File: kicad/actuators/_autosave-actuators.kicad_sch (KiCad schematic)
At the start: 41 parts, among them J10 Conn_01x03, J11 Conn_01x03, J12 Conn_01x03, J13 Conn_01x03, J18 6V_IN, J19 3V3_IN, J5 Conn_02x03_Odd_Even, J6 Conn_01x06, J7 Conn_01x03, J8 Conn_01x03, J9 Conn_01x03, U5 SN65HVD230, U6 STM32G431R6Tx, U7 DRV8874PWPR

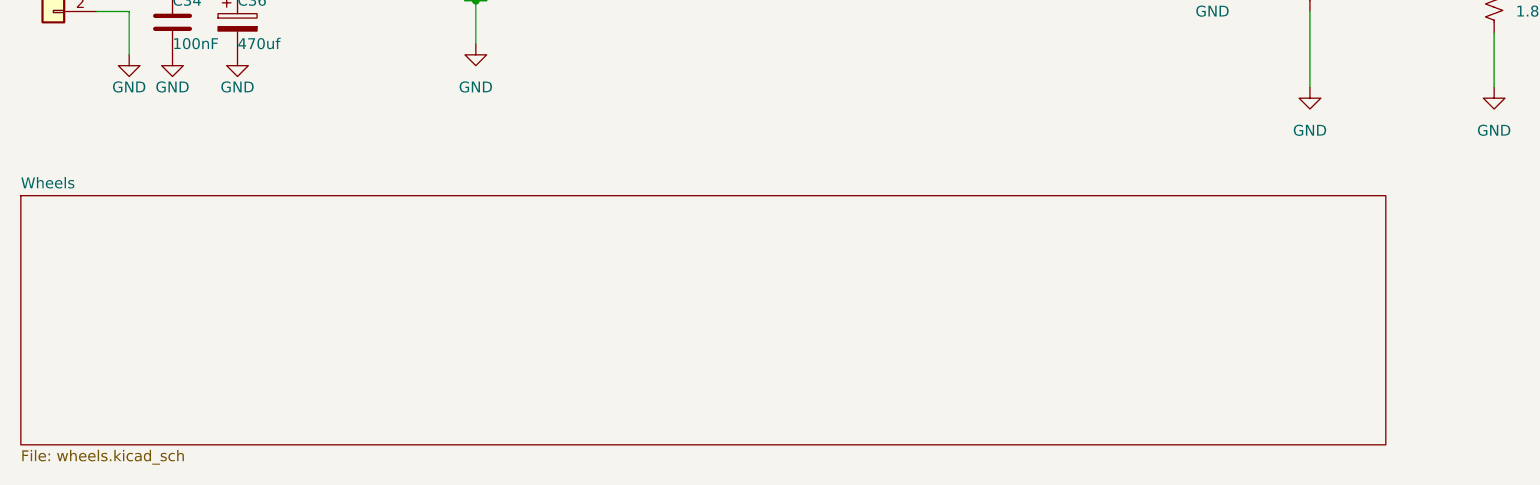
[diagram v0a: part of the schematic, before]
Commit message: working on the schematic of the actuator & motor board, schematic almost done
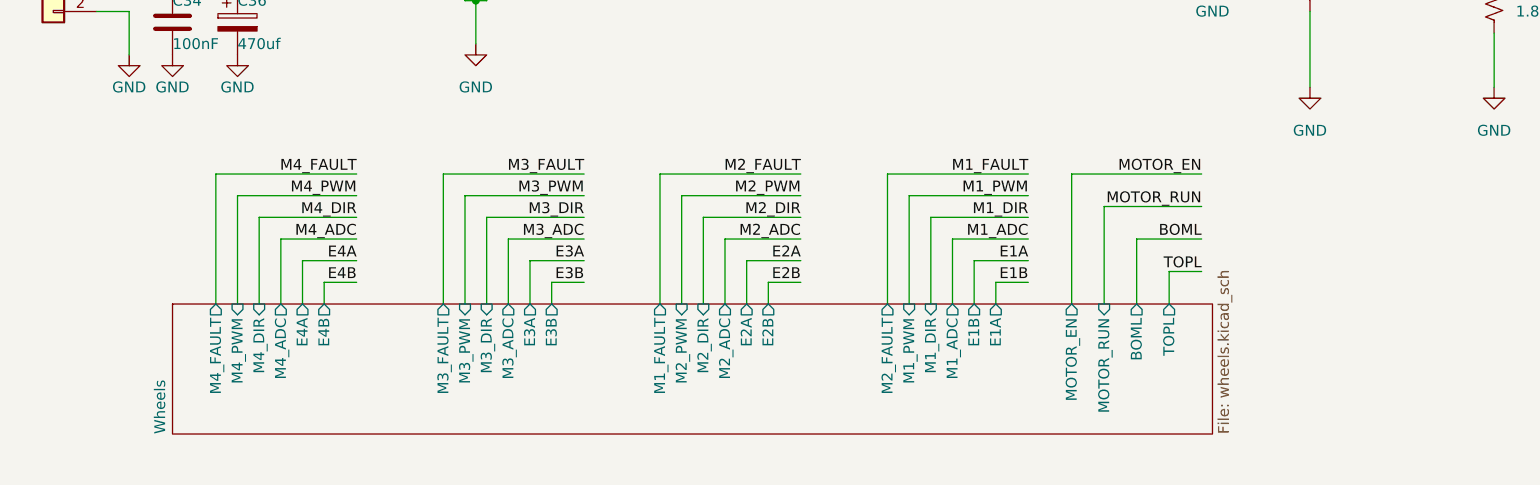
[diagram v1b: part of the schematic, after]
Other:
- sheet Wheels ports: added BOML, E1A, E1B, E2A, E2B, E3A, E3B, E4A, E4B, M1_ADC, M1_DIR, M1_FAULT, M1_PWM, M2_ADC, M2_DIR, M2_FAULT, M2_PWM, M3_ADC, M3_DIR, M3_FAULT, M3_PWM, M4_ADC, M4_DIR, M4_FAULT, M4_PWM, MOTOR_EN, MOTOR_RUN, TOPL; removed none

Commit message: completed the actuator pcb
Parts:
- removed R18: 10k, symbol Device:R_US
- added J3: Jumper, Connector_PinHeader_2.54mm:PinHeader_1x02_P2.54mm_Vertical, symbol Connector_Generic:Conn_01x02
- added SW1: SW_Push, Button_Switch_SMD:SW_SPST_PTS647_Sx38, symbol Switch:SW_Push
- added TP1: Boot, TestPoint:TestPoint_Pad_1.5x1.5mm, symbol Connector:TestPoint
- C1: renamed from C25; footprint (none) -> Capacitor_SMD:C_0603_1608Metric
- C19: renamed from C29; footprint Capacitor_SMD:C_0603_1608Metric -> Capacitor_SMD:CP_Elec_5x5.3
- C2: renamed from C33; footprint (none) -> Capacitor_SMD:C_0603_1608Metric
- C3: renamed from C34; footprint (none) -> Capacitor_SMD:C_0603_1608Metric
- C4: renamed from C35; footprint (none) -> Capacitor_SMD:CP_Elec_10x10.5
- C5: renamed from C36; footprint (none) -> Capacitor_SMD:CP_Elec_10x10.5
- J1: renamed from J19; footprint (none) -> Connector_AMASS:AMASS_XT60-M_1x02_P7.20mm_Vertical
- J10: renamed from J11; footprint (none) -> Connector_PinSocket_2.54mm:PinSocket_1x03_P2.54mm_Vertical
- J11: renamed from J13; footprint (none) -> Connector_PinSocket_2.54mm:PinSocket_1x03_P2.54mm_Vertical
- J12: renamed from J7; footprint (none) -> Connector_PinSocket_2.54mm:PinSocket_1x03_P2.54mm_Vertical
- J2: renamed from J18; footprint (none) -> Connector_AMASS:AMASS_XT60-M_1x02_P7.20mm_Vertical
- J4: renamed from J5; footprint (none) -> Connector_PinHeader_2.54mm:PinHeader_2x03_P2.54mm_Vertical
- J6: renamed from J9; footprint (none) -> Connector_PinSocket_2.54mm:PinSocket_1x03_P2.54mm_Vertical
- J7: renamed from J10; footprint (none) -> Connector_PinSocket_2.54mm:PinSocket_1x03_P2.54mm_Vertical
- J8: renamed from J12; footprint (none) -> Connector_PinSocket_2.54mm:PinSocket_1x03_P2.54mm_Vertical
- J9: renamed from J8; footprint (none) -> Connector_PinSocket_2.54mm:PinSocket_1x03_P2.54mm_Vertical
- R1: renamed from R17; footprint (none) -> Resistor_SMD:R_0603_1608Metric
- R6: renamed from R23; footprint (none) -> Resistor_SMD:R_0603_1608Metric
- R7: renamed from R24; footprint (none) -> Resistor_SMD:R_0603_1608Metric
- renumbered C21 to C10, C22 to C11, C23 to C12, C24 to C13, C30 to C14, C31 to C15, C26 to C16, C27 to C17, C28 to C18, C17 to C6, C18 to C7, C19 to C8, C20 to C9, J6 to J5, R19 to R2, R20 to R3, R21 to R4, R22 to R5, U6 to U1, U7 to U2, U5 to U3
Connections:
- net M1_ENA is gone; now on net M5_ENA: U2.3 (nSLEEP)
- net BOML: now also U1.3 (PC14)
- net CAN-D: now also U1.62 (PB9)
- net CAN-R: now also J3.2 (Pin_2)
- net E1A: now also U1.12 (PA0)
- net E1B: now also U1.13 (PA1)
- net E2A: now also U1.20 (PA6)
- net E2B: now also U1.21 (PA7)
- net E3A: now also U1.59 (PB6); no longer J5.3 (Pin_3)
- net E3B: now also U1.60 (PB7); no longer J5.4 (Pin_4)
- net E4A: now also U1.38 (PC6)
- net E4B: now also U1.39 (PC7)
- net GND: now also SW1.1
- net M1_ADC: now also U1.8 (PC0); no longer R5.1, U2.6 (IPROPI)
- net M1_DIR: now also U1.30 (PB10); no longer U2.2 (PH/IN2)
- net M1_FAULT: now also U1.52 (PC10); no longer R4.2, U2.4 (nFAULT)
- net M1_PWM: now also U1.42 (PA8); no longer U2.1 (EN/IN1)
- net M2_ADC: now also U1.9 (PC1)
- net M2_DIR: now also U1.33 (PB11)
- net M2_FAULT: now also U1.53 (PC11)
- net M2_PWM: now also U1.43 (PA9)
- net M3_ADC: now also U1.10 (PC2)
- net M3_DIR: now also U1.34 (PB12)
- net M3_FAULT: now also U1.54 (PC12)
- net M3_PWM: now also U1.44 (PA10)
- net M4_ADC: now also U1.11 (PC3)
- net M4_DIR: now also U1.35 (PB13)
- net M4_FAULT: now also U1.55 (PD2)
- net M4_PWM: now also U1.45 (PA11)
- net MOTOR_EN: now also U1.58 (PB5)
- net MOTOR_RUN: now also U1.56 (PB3)
- net SR1: now also U1.14 (PA2)
- net SR2: now also U1.17 (PA3)
- net SR3: now also U1.18 (PA4)
- net SR4: now also U1.19 (PA5)
- net SR5: now also U1.46 (PA12)
- net SR6: now also U1.51 (PA15)
- net TOPL: now also U1.2 (PC13)
- net at C1.1, R1.2, U1.7 (PG10): now also SW1.2
- net M5_FAULT: now reaches U1.22 (PC4)
- net M5_FAULT: now also R4.2, U2.4 (nFAULT)
- net M5_ENA: now reaches U1.23 (PC5)
- net E5A: now reaches U1.24 (PB0)
- net E5A: now also J5.3 (Pin_3)
- net E5B: now reaches U1.25 (PB1)
- net E5B: now also J5.4 (Pin_4)
- net M5_DIR: now reaches U1.26 (PB2)
- net M5_DIR: now also U2.2 (PH/IN2)
- net M5_PWM: now reaches U1.36 (PB14)
- net M5_PWM: now also U2.1 (EN/IN1)
- net nSLEEP: now reaches U1.41 (PC9)
- net M5_ADC: now reaches U1.57 (PB4)
- net M5_ADC: now also R5.1, U2.6 (IPROPI)
- net at U1.61 (PB8): now also J3.1 (Pin_1), TP1.1
- net M3A renamed M5A
- net M3B renamed M5B
- no-connect marks 1 -> 6
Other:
- sheet Wheels ports: added nSLEEP; removed none
